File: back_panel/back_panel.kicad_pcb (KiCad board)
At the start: 2 copper layers, 82.8 x 28.8 mm, 8 parts

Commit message: minor change from plotting gerbers
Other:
- board text added: "unbal2bal back_panel r0 github.com/gkeeth/unbal2bal 2022-06-17"
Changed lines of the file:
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@@
       (outputformat 1)
       (mirror false)
-      (drillshape 1)
+      (drillshape 0)
       (scaleselection 1)
-      (outputdirectory "")
+      (outputdirectory "../fab/back_panel/")
     )
   )
@@
     (effects (font (size 1 1) (thickness 0.15)) (justify mirror))
   )
+  (gr_text "unbal2bal back_panel r0\ngithub.com/gkeeth/unbal2bal\n2022-06-17" (at 190 102) (layer "B.SilkS")
+    (effects (font (size 1 1) (thickness 0.15)) (justify left mirror))
+  )
   (zone (net 1) (net_name "GND") (layers F&B.Cu) (hatch edge 0.508)

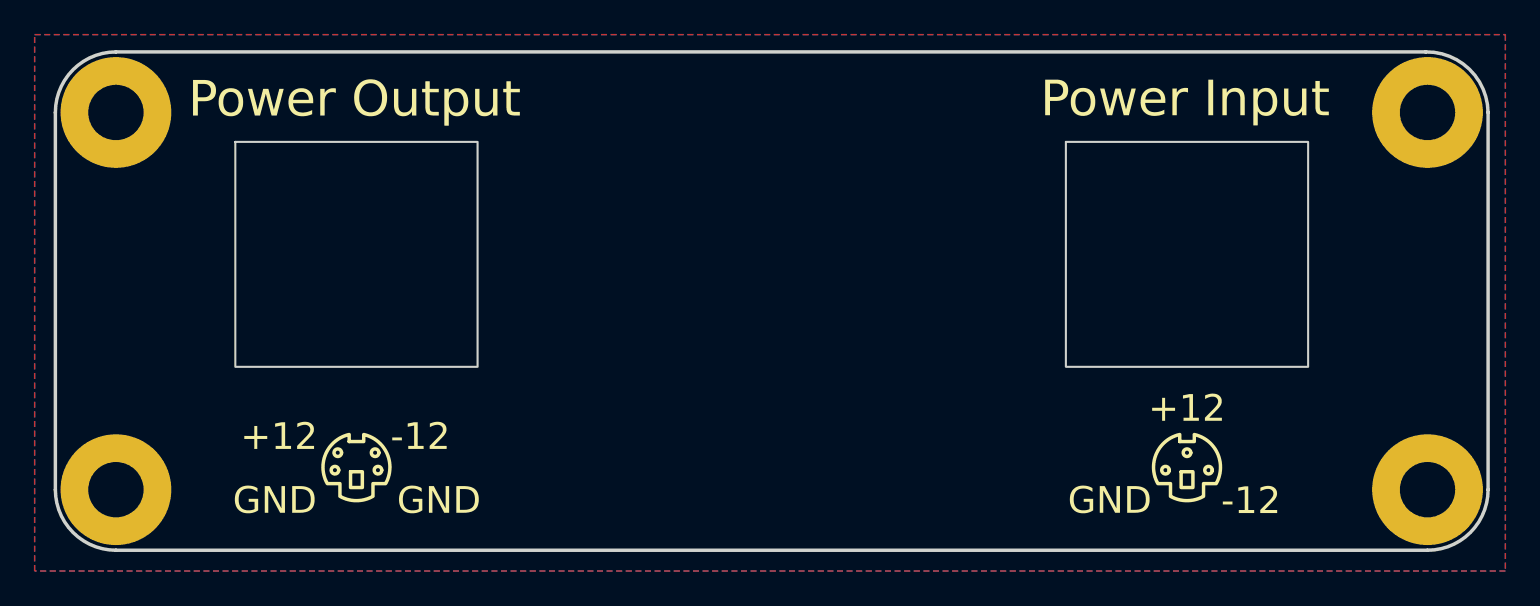
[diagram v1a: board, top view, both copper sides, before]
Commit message: swap to power DIN connectors for back panel
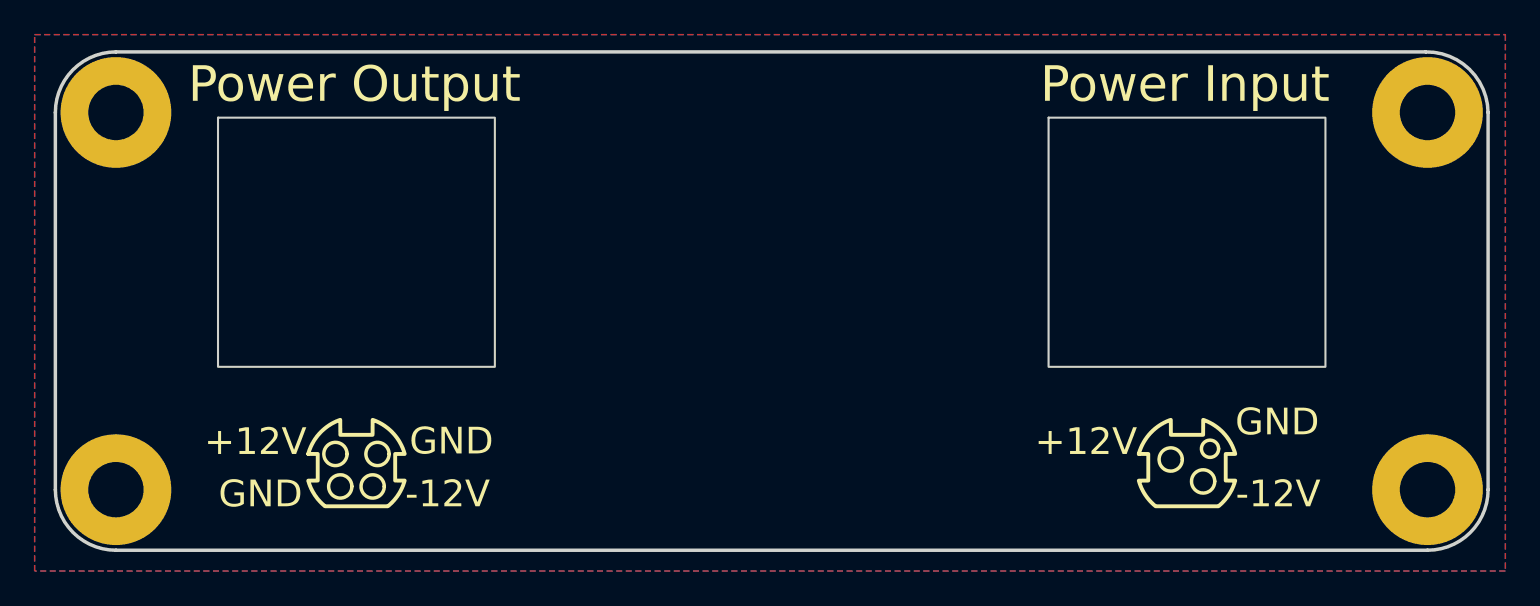
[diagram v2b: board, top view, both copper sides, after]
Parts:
- REF**: value Panel_Mini-DIN_Kycon_KMDGX-xS-BS -> Panel_Power-DIN_CUI_PD-x0S; footprint Panel_Cutouts:Panel_Mini-DIN_Kycon_KMDGX-xS-BS -> Panel_Cutouts:Panel_Power-DIN_CUI_PD-x0S
- REFe: renamed from REF**; value Panel_Mini-DIN_Kycon_KMDGX-xS-BS -> Panel_Power-DIN_CUI_PD-x0S; footprint Panel_Cutouts:Panel_Mini-DIN_Kycon_KMDGX-xS-BS -> Panel_Cutouts:Panel_Power-DIN_CUI_PD-x0S
- svg2mod: footprint Panel_Cutouts:mini-din-3 -> Panel_Cutouts:power-din-3
- svg2mod: footprint Panel_Cutouts:mini-din-4 -> Panel_Cutouts:power-din-4
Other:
- board text added: "unbal2bal back_panel r1 github.com/gkeeth/unbal2bal 2022-10-08"
- board text removed: "unbal2bal back_panel r0 github.com/gkeeth/unbal2bal 2022-06-17"

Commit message: swap to round cutouts for power-din connectors
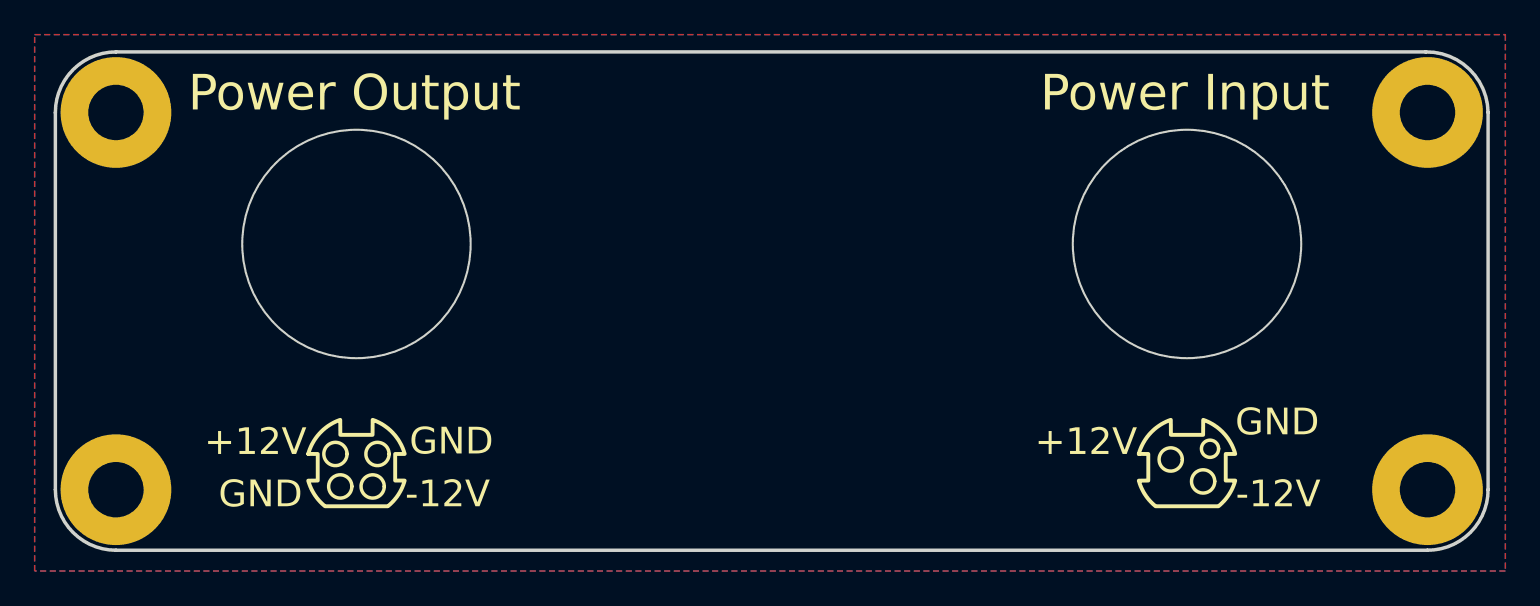
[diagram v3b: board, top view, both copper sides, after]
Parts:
- renumbered REFe to REF**
